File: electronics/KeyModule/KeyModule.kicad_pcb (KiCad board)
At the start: 2 copper layers, 16.5 x 100 mm, 17 parts, among them SW1 SW_Push, SW2 SW_Push, SW3 SW_Push, SW4 SW_Push, SW5 SW_Push, U1 74HC165

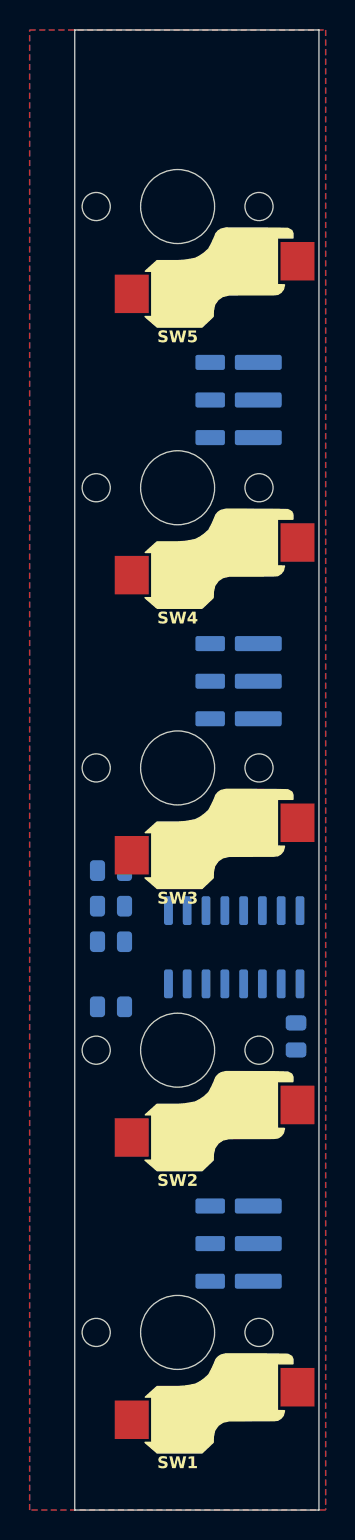
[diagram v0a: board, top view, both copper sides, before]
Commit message: Route the key module
All copper on the back except five 0805 pull-downs, which move to the
front between switches where nothing else lives. Row 2 of the
interconnect becomes CLK / PL / DATA: DATA on the bottom pin is the
only pin whose track can leave the pad without crossing a pass-through.
Choc hotswap sockets, their pads and outline move to the back of the
switch footprint, where the socket physically mounts. GND is the zone
on both layers, stitched by five vias. kicad-cli DRC with schematic
parity: no violations, no unconnected items.

Co-Authored-By: Claude Fable 5.1 <noreply@anthropic.com>
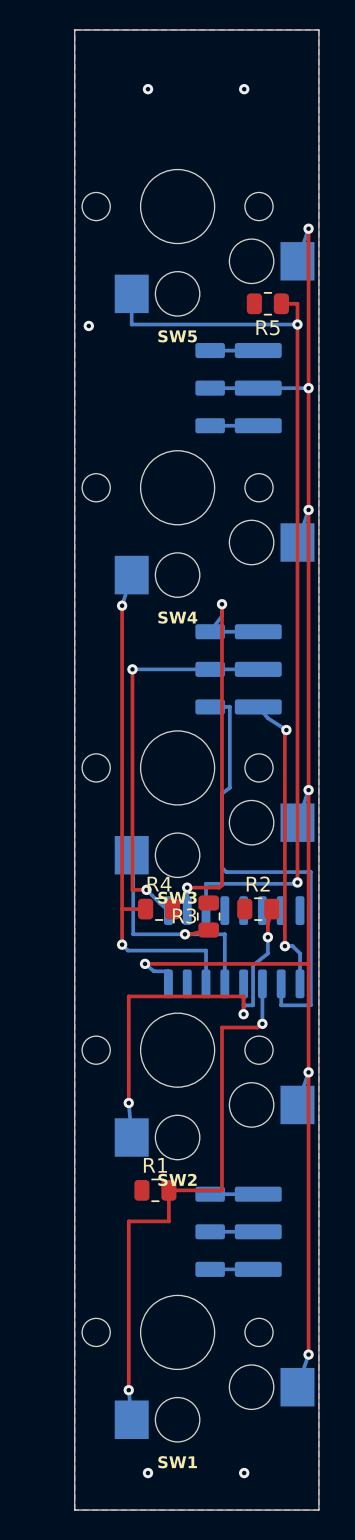
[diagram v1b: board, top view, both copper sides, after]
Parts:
- R1, R2, R3, R4, R5: moved to F.Cu
- moved R5 39.7 mm to (83.6, 58.5), turned to 180 degrees
- moved R1 14.1 mm to (76.0, 118.4), turned to 0 degrees
- moved R2 11.9 mm to (83.0, 99.4)
- moved R3 6.82 mm to (79.6, 99.9), turned to 90 degrees
- moved R4 3.26 mm to (76.2, 99.4)
- moved J_LEFT1 0.80 mm to (79.7, 64.2)
- moved J_LEFT2 0.80 mm to (79.7, 83.2)
- moved J_LEFT3 0.80 mm to (79.7, 121.2)
- moved J_RIGHT1 0.80 mm to (83.0, 64.2)
- moved J_RIGHT2 0.80 mm to (83.0, 83.2)
- moved J_RIGHT3 0.80 mm to (83.0, 121.2)
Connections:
- J_LEFT2 pad 2: /DATA_IN -> /PL
- J_LEFT2 pad 3: /PL -> /DATA_IN
- J_RIGHT2 pad 2: /DATA_OUT -> /PL
- J_RIGHT2 pad 3: /PL -> /DATA_OUT
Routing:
- net +3.3V: track 0.00 -> 108.0 mm, vias 0 -> 7
- net Net-(U1-D4): track 0.00 -> 61.5 mm, vias 0 -> 2
- net Net-(U1-D0): track 0.00 -> 38.3 mm, vias 0 -> 2
- net Net-(U1-D3): track 0.00 -> 34.7 mm, vias 0 -> 2
- net /DATA_IN: track 0.00 -> 31.0 mm
- net /CLK: track 0.00 -> 28.3 mm, vias 0 -> 2
- net Net-(U1-D1): track 0.00 -> 28.2 mm, vias 0 -> 3
- net /PL: track 0.00 -> 26.4 mm, vias 0 -> 2
- net /DATA_OUT: track 0.00 -> 20.4 mm, vias 0 -> 2
- net Net-(U1-D2): track 0.00 -> 16.5 mm, vias 0 -> 1
- net GND: track 0.00 -> 3.25 mm, vias 0 -> 5
- net /SDA: track 0.00 -> 3.25 mm
- net /SCL: track 0.00 -> 3.25 mm
- net /LED: track 0.00 -> 3.25 mm
- net +5V: track 0.00 -> 3.25 mm

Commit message: Add 100 nF decoupling for the 165 and export fab files
Electronics.md promised decoupling and the schematic had none. C1 sits
on the front beside U1, fed from the +3.3V branch. ERC clean, DRC with
parity clean. fab/KeyModule-gerbers.zip holds gerbers and drills for
this revision.

Co-Authored-By: Claude Fable 5.1 <noreply@anthropic.com>
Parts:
- added C1: 100nF, Capacitor_SMD:C_0805_2012Metric, F.Cu at (78.5, 104.2)
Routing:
- net +3.3V: track 108.0 -> 109.1 mm
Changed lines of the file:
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@@
 		)
 	)
+	(footprint "Capacitor_SMD:C_0805_2012Metric"
+		(layer "F.Cu")
+		(at 78.5 104.2)
+		(descr "Capacitor SMD 0805 (2012 Metric), square (rectangular) end terminal, IPC-7351 nominal, (Body size source: IPC-SM-782 page 76, https://www.pcb-3d.com/wordpress/wp-content/uploads/ipc-sm-782a_amendment_1_and_2.pdf, https://docs.google.com/spreadsheets/d/1BsfQQcO9C6DZCsRaXUlFlo91Tg2WpOkGARC1WS5S8t0/edit?usp=sharing)")
+		(tags "capacitor")
+		(property "Reference" "C1"
+			(at 0 -1.68 0)
+			(layer "F.SilkS")
+			(effects
+				(font
+					(size 1 1)
+					(thickness 0.15)
+				)
+			)
+		)
+		(property "Value" "100nF"
+			(at 0 1.68 0)
+			(layer "F.Fab")
+			(effects
+				(font
+					(size 1 1)
+					(thickness 0.15)
+				)
+			)
+		)
+		(property "Datasheet" ""
+			(at 0 0 0)
+			(layer "F.Fab")
+			(hide yes)
+			(effects
+				(font
+					(size 1.27 1.27)
+				)
+			)
+		)
+		(property "Description" "Decoupling for the 74HC165"
+			(at 0 0 0)
+			(layer "F.Fab")
+			(hide yes)
+			(effects
+				(font
+					(size 1.27 1.27)
+				)
+			)
+		)
+		(property "KiLib_Generator" "SMD_2terminal_chip_molded"
+			(at 0 0 0)
+			(layer "F.SilkS")
+			(hide yes)
+			(effects
+				(font
+					(size 1 1)
+					(thickness 0.15)
+				)
+			)
+		)
+		(property "Ideal Part Number" ""
+			(at 0 0 0)
+			(layer "F.Fab")
+			(hide yes)
+			(effects
+				(font
+					(size 1 1)
+					(thickness 0.15)
+				)
+			)
+		)
+		(property "Order Link" ""
+			(at 0 0 0)
+			(layer "F.Fab")
+			(hide yes)
+			(effects
+				(font
+					(size 1 1)
+					(thickness 0.15)
+				)
+			)
+		)
+		(property "Vendor" ""
+			(at 0 0 0)
+			(layer "F.Fab")
+			(hide yes)
+			(effects
+				(font
+					(size 1 1)
+					(thickness 0.15)
+				)
+			)
+		)
+		(sheetname "/")
+		(sheetfile "KeyModule.kicad_sch")
+		(attr smd)
+		(duplicate_pad_numbers_are_jumpers no)
+		(fp_line
+			(start -0.261252 -0.735)
+			(end 0.261252 -0.735)
+			(stroke
+				(width 0.12)
+				(type solid)
+			)
+			(layer "F.SilkS")
+		)
+		(fp_line
+			(start -0.261252 0.735)
+			(end 0.261252 0.735)
+			(stroke
+				(width 0.12)
+				(type solid)
+			)
+			(layer "F.SilkS")
+		)
+		(fp_rect
+			(start -1.7 -0.98)
+			(end 1.7 0.98)
+			(stroke
+				(width 0.05)
+				(type solid)
+			)
+			(fill no)
+			(layer "F.CrtYd")
+		)
+		(fp_rect
+			(start -1 -0.625)
+			(end 1 0.625)
+			(stroke
+				(width 0.1)
+				(type solid)
+			)
+			(fill no)
+			(layer "F.Fab")
+		)
+		(fp_text user "${REFERENCE}"
+			(at 0 0 0)
+			(layer "F.Fab")
+			(effects
+				(font
+					(size 0.5 0.5)
+					(thickness 0.08)
+				)
+			)
+		)
+		(pad "1" smd roundrect
+			(at -0.95 0)
+			(size 1 1.45)
+			(layers "F.Cu" "F.Mask" "F.Paste")
+			(roundrect_rratio 0.25)
+			(net "+3.3V")
+			(pintype "passive")
+		)
+		(pad "2" smd roundrect
+			(at 0.95 0)
+			(size 1 1.45)
+			(layers "F.Cu" "F.Mask" "F.Paste")
+			(roundrect_rratio 0.25)
+			(net "GND")
+			(pintype "passive")
+		)
+		(embedded_fonts no)
+		(model "${KICAD10_3DMODEL_DIR}/Capacitor_SMD.3dshapes/C_0805_2012Metric.step"
+			(offset
+				(xyz 0 0 0)
+			)
+			(scale
+				(xyz 1 1 1)
+			)
+			(rotate
+				(xyz 0 0 0)
+			)
+		)
+	)
 	(footprint "Resistor_SMD:R_0805_2012Metric"
 		(layer "F.Cu")
@@
 		(width 0.25)
 		(layer "F.Cu")
+		(net "+3.3V")
+	)
+	(segment
+		(start 77.55 104.2)
+		(end 77.55 103.1)
+		(width 0.25)
+		(layer "F.Cu")
